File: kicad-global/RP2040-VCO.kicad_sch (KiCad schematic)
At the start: 57 parts, among them J1 Out, J2 Conn_01x06_Female, J3 Conn_01x06_Male, J4 Conn_01x08_Female, J5 Conn_01x08_Male, J6 V/oct, J7 Inv CV, J8 Power Input, SW1 SW_MEC_LOW_PROF_LED, SW2 SW_SPDT, U1 TL074, U2 Seed_XIAO_RP2040, U3 AP2210K-5.0TRG1

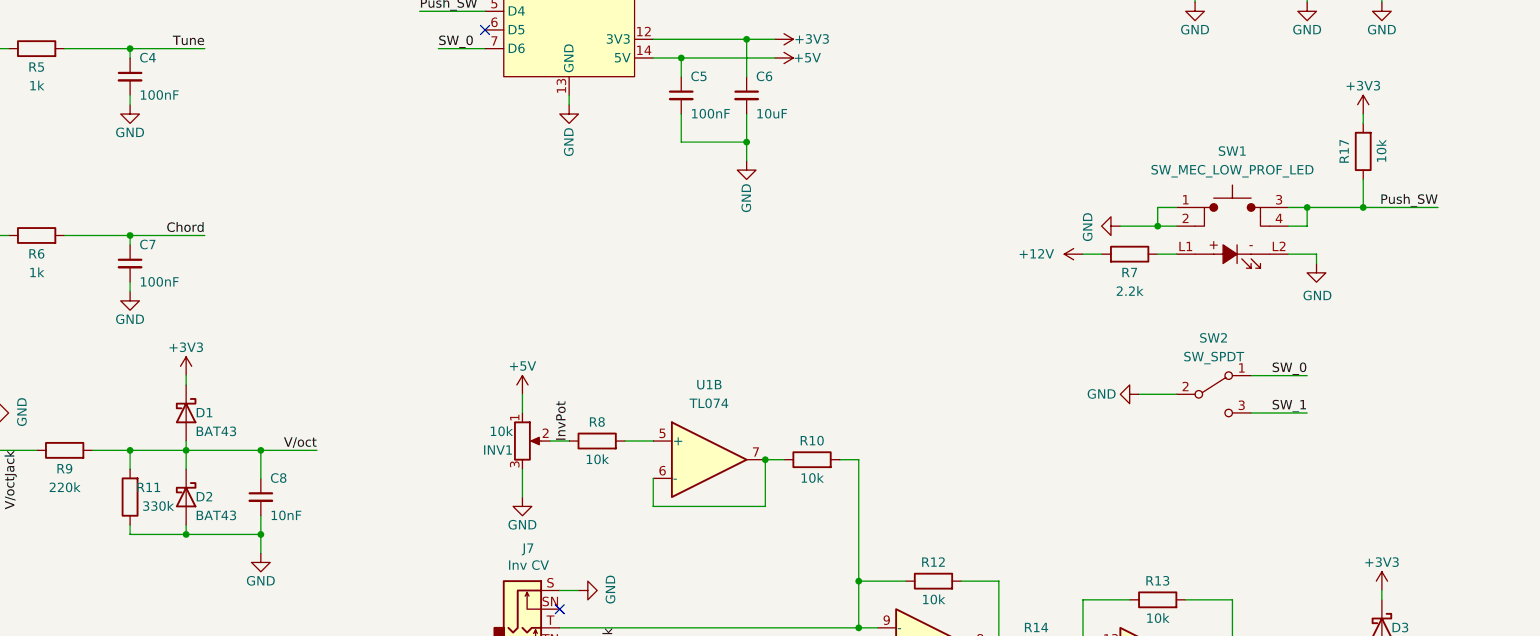
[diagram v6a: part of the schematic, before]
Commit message: update pcb to v1.2 to fix switch issue with switch LED
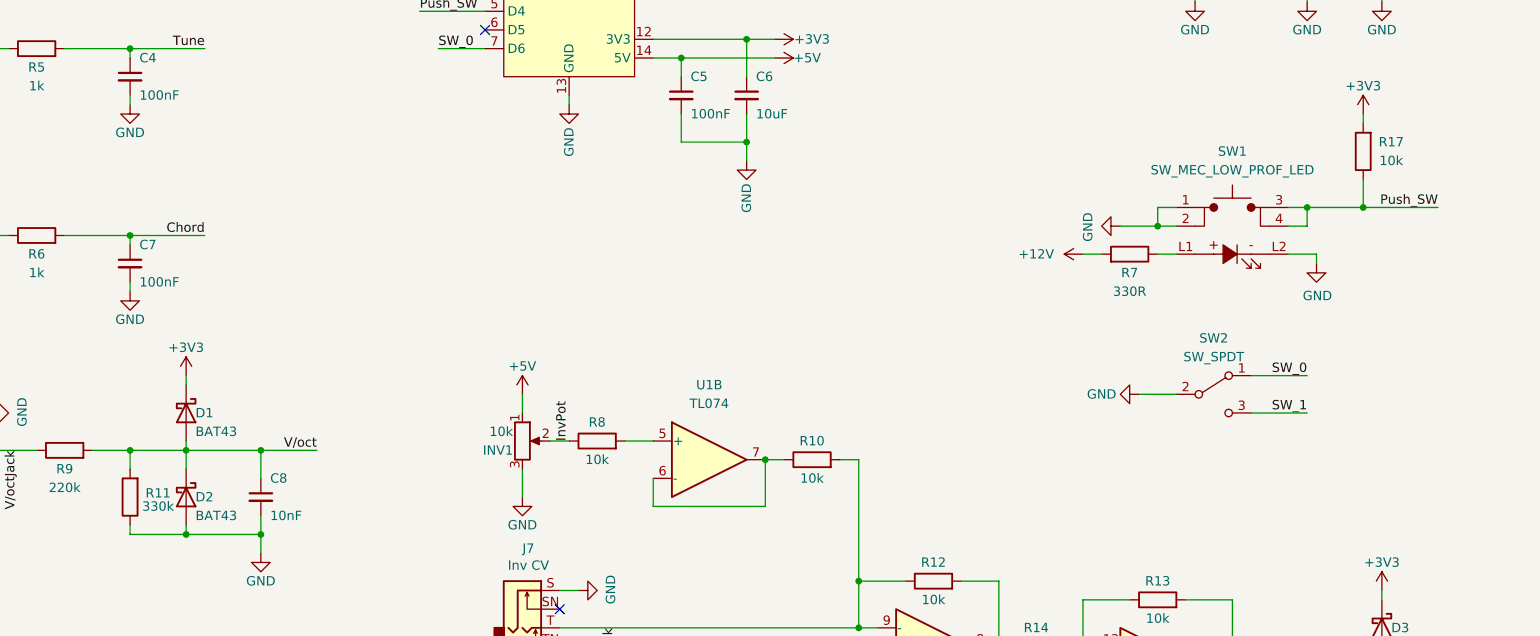
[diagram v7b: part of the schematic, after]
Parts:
- R7: value 2.2k -> 330R; MFP RC0805FR-132K2L -> RC0805FR-10330RL
- U3: MFP (none) -> AP2210K-5.0TRG1; MPN AP2210K-5.0TRG1 -> (none)
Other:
- company: (none) -> Bleep Sound
- title: (none) -> RP2040 VCO
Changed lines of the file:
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@@
 (kicad_sch (version 20230121) (generator eeschema)
   (paper "A4")
+  (title_block
+    (title "RP2040 VCO")
+    (date "2023-10-11")
+    (rev "1.2")
+    (company "Bleep Sound")
+  )
   (junction (at 123.19 175.26) (diameter 0) (color 0 0 0 0)
   )
@@
   (junction (at 143.51 187.96) (diameter 0) (color 0 0 0 0)
   )
-  (junction (at 214.63 81.28) (diameter 0) (color 0 0 0 0)
-  )
   (junction (at 130.81 58.42) (diameter 0) (color 0 0 0 0)
   )
@@
   (junction (at 236.22 46.99) (diameter 0) (color 0 0 0 0)
   )
+  (junction (at 214.63 81.28) (diameter 0) (color 0 0 0 0)
+  )
   (junction (at 26.67 33.02) (diameter 0) (color 0 0 0 0)
   )
@@
     (stroke (width 0) (type default))
   )
+  (wire (pts (xy 214.63 81.28) (xy 224.79 81.28))
+    (stroke (width 0) (type default))
+  )
   (wire (pts (xy 207.01 104.14) (xy 199.39 104.14))
     (stroke (width 0) (type default))
@@
     (stroke (width 0) (type default))
   )
-  (wire (pts (xy 214.63 68.58) (xy 214.63 69.85))
-    (stroke (width 0) (type default))
-  )
   (wire (pts (xy 143.51 115.57) (xy 146.05 115.57))
     (stroke (width 0) (type default))
@@
     (stroke (width 0) (type default))
   )
+  (wire (pts (xy 214.63 68.58) (xy 214.63 69.85))
+    (stroke (width 0) (type default))
+  )
   (wire (pts (xy 166.37 175.26) (xy 168.91 175.26))
     (stroke (width 0) (type default))
@@
     (stroke (width 0) (type default))
   )
+  (wire (pts (xy 214.63 77.47) (xy 214.63 81.28))
+    (stroke (width 0) (type default))
+  )
   (wire (pts (xy 148.59 143.51) (xy 146.05 143.51))
     (stroke (width 0) (type default))
@@
     (stroke (width 0) (type default))
   )
-  (wire (pts (xy 214.63 81.28) (xy 224.79 81.28))
-    (stroke (width 0) (type default))
-  )
   (wire (pts (xy 39.37 182.88) (xy 45.72 182.88))
     (stroke (width 0) (type default))
@@
     (stroke (width 0) (type default))
   )
-  (wire (pts (xy 214.63 77.47) (xy 214.63 81.28))
-    (stroke (width 0) (type default))
-  )
   (wire (pts (xy 236.22 46.99) (xy 236.22 36.83))
     (stroke (width 0) (type default))
@@
       (effects (font (size 1.27 1.27)))
     )
-    (property "Value" "2.2k" (at 182.88 92.71 90)
+    (property "Value" "330R" (at 182.88 92.71 90)
       (effects (font (size 1.27 1.27)))
     )
@@
       (effects (font (size 1.27 1.27)) hide)
     )
-    (property "MFP" "RC0805FR-132K2L" (at 182.88 87.63 0)
+    (property "MFP" "RC0805FR-10330RL" (at 182.88 87.63 0)
       (effects (font (size 1.27 1.27)) hide)
     )
@@
     )
   )
+  (symbol (lib_id "Device:R") (at 214.63 73.66 180) (unit 1)
+    (in_bom yes) (on_board yes) (dnp no)
+    (property "Reference" "R17" (at 218.44 72.39 0)
+      (effects (font (size 1.27 1.27)))
+    )
+    (property "Value" "10k" (at 218.44 74.93 0)
+      (effects (font (size 1.27 1.27)))
+    )
+    (property "Footprint" "Resistor_SMD:R_0805_2012Metric_Pad1.20x1.40mm_HandSolder" (at 216.408 73.66 90)
+      (effects (font (size 1.27 1.27)) hide)
+    )
+    (property "Datasheet" "~" (at 214.63 73.66 0)
+      (effects (font (size 1.27 1.27)) hide)
+    )
+    (property "Comment " "1/4W, 1%" (at 214.63 73.66 0)
+      (effects (font (size 1.27 1.27)) hide)
+    )
+    (property "MFN" "YAGEO" (at 214.63 73.66 0)
+      (effects (font (size 1.27 1.27)) hide)
+    )
+    (property "MFP" "RC0805FR-1010KL" (at 214.63 73.66 0)
+      (effects (font (size 1.27 1.27)) hide)
+    )
+    (pin "1")
+    (pin "2")
+    (instances
+      (project "RP2040-VCO"
+        (path "/fea7c5d1-76d6-41a0-b5e3-29889dbb8ce0"
+          (reference "R17") (unit 1)
+        )
+      )
+    )
+  )
   (symbol (lib_id "Amplifier_Operational:TL074") (at 125.73 115.57 0) (unit 2)
     (in_bom yes) (on_board yes) (dnp no) (fields_autoplaced)
@@
     )
   )
+  (symbol (lib_id "power:+3V3") (at 214.63 68.58 0) (unit 1)
+    (in_bom yes) (on_board yes) (dnp no)
+    (property "Reference" "#PWR048" (at 214.63 72.39 0)
+      (effects (font (size 1.27 1.27)) hide)
+    )
+    (property "Value" "+3V3" (at 214.63 64.77 0)
+      (effects (font (size 1.27 1.27)))
+    )
+    (property "Footprint" "" (at 214.63 68.58 0)
+      (effects (font (size 1.27 1.27)) hide)
+    )
+    (property "Datasheet" "" (at 214.63 68.58 0)
+      (effects (font (size 1.27 1.27)) hide)
+    )
+    (pin "1")
+    (instances
+      (project "RP2040-VCO"
+        (path "/fea7c5d1-76d6-41a0-b5e3-29889dbb8ce0"
+          (reference "#PWR048") (unit 1)
+        )
+      )
+    )
+  )
   (symbol (lib_id "power:+5V") (at 266.7 87.63 270) (mirror x) (unit 1)
     (in_bom yes) (on_board yes) (dnp no)
@@
   (symbol (lib_id "Device:R") (at 46.99 120.65 180) (unit 1)
     (in_bom yes) (on_board yes) (dnp no)
-    (property "Reference" "R11" (at 49.53 119.38 0)
-      (effects (font (size 1.27 1.27)))
+    (property "Reference" "R11" (at 50.8 119.38 0)
+      (effects (font (size 1.27 1.27)) (justify bottom))
     )
     (property "Value" "330k" (at 50.8 121.92 0)
@@
     )
   )
-  (symbol (lib_id "Device:R") (at 214.63 73.66 180) (unit 1)
-    (in_bom yes) (on_board yes) (dnp no)
-    (property "Reference" "R17" (at 212.09 73.66 90)
-      (effects (font (size 1.27 1.27)))
-    )
-    (property "Value" "10k" (at 217.17 73.66 90)
-      (effects (font (size 1.27 1.27)))
-    )
-    (property "Footprint" "Resistor_SMD:R_0805_2012Metric_Pad1.20x1.40mm_HandSolder" (at 216.408 73.66 90)
-      (effects (font (size 1.27 1.27)) hide)
-    )
-    (property "Datasheet" "~" (at 214.63 73.66 0)
-      (effects (font (size 1.27 1.27)) hide)
-    )
-    (property "Comment " "1/4W, 1%" (at 214.63 73.66 0)
-      (effects (font (size 1.27 1.27)) hide)
-    )
-    (property "MFN" "YAGEO" (at 214.63 73.66 0)
-      (effects (font (size 1.27 1.27)) hide)
-    )
-    (property "MFP" "RC0805FR-1010KL" (at 214.63 73.66 0)
-      (effects (font (size 1.27 1.27)) hide)
-    )
-    (pin "1")
-    (pin "2")
-    (instances
-      (project "RP2040-VCO"
-        (path "/fea7c5d1-76d6-41a0-b5e3-29889dbb8ce0"
-          (reference "R17") (unit 1)
-        )
-      )
-    )
-  )
   (symbol (lib_id "power:+12V") (at 100.33 168.91 0) (unit 1)
     (in_bom yes) (on_board yes) (dnp no)
@@
       (effects (font (size 1.27 1.27)) (justify left) hide)
     )
-    (property "MPN" "AP2210K-5.0TRG1" (at 167.64 182.88 0)
-      (effects (font (size 1.27 1.27)) (justify left) hide)
+    (property "MFP" "AP2210K-5.0TRG1" (at 143.51 177.8 0)
+      (effects (font (size 1.27 1.27)) hide)
     )
     (pin "1")
@@
     )
   )
-  (symbol (lib_id "power:+3V3") (at 214.63 68.58 0) (unit 1)
-    (in_bom yes) (on_board yes) (dnp no)
-    (property "Reference" "#PWR048" (at 214.63 72.39 0)
-      (effects (font (size 1.27 1.27)) hide)
-    )
-    (property "Value" "+3V3" (at 214.63 64.77 0)
-      (effects (font (size 1.27 1.27)))
-    )
-    (property "Footprint" "" (at 214.63 68.58 0)
-      (effects (font (size 1.27 1.27)) hide)
-    )
-    (property "Datasheet" "" (at 214.63 68.58 0)
-      (effects (font (size 1.27 1.27)) hide)
-    )
-    (pin "1")
-    (instances
-      (project "RP2040-VCO"
-        (path "/fea7c5d1-76d6-41a0-b5e3-29889dbb8ce0"
-          (reference "#PWR048") (unit 1)
-        )
-      )
-    )
-  )
   (symbol (lib_id "Device:C_Small") (at 166.37 180.34 0) (mirror y) (unit 1)
     (in_bom yes) (on_board yes) (dnp no)
@@
       (effects (font (size 1.27 1.27)) hide)
     )
-    (property "Datasheet" "~" (at 194.31 106.68 0)
+    (property "Datasheet" "https://www.taydaelectronics.com/mini-toggle-switch-1m-series-spdt-on-off-on.html" (at 194.31 106.68 0)
       (effects (font (size 1.27 1.27)) hide)
     )

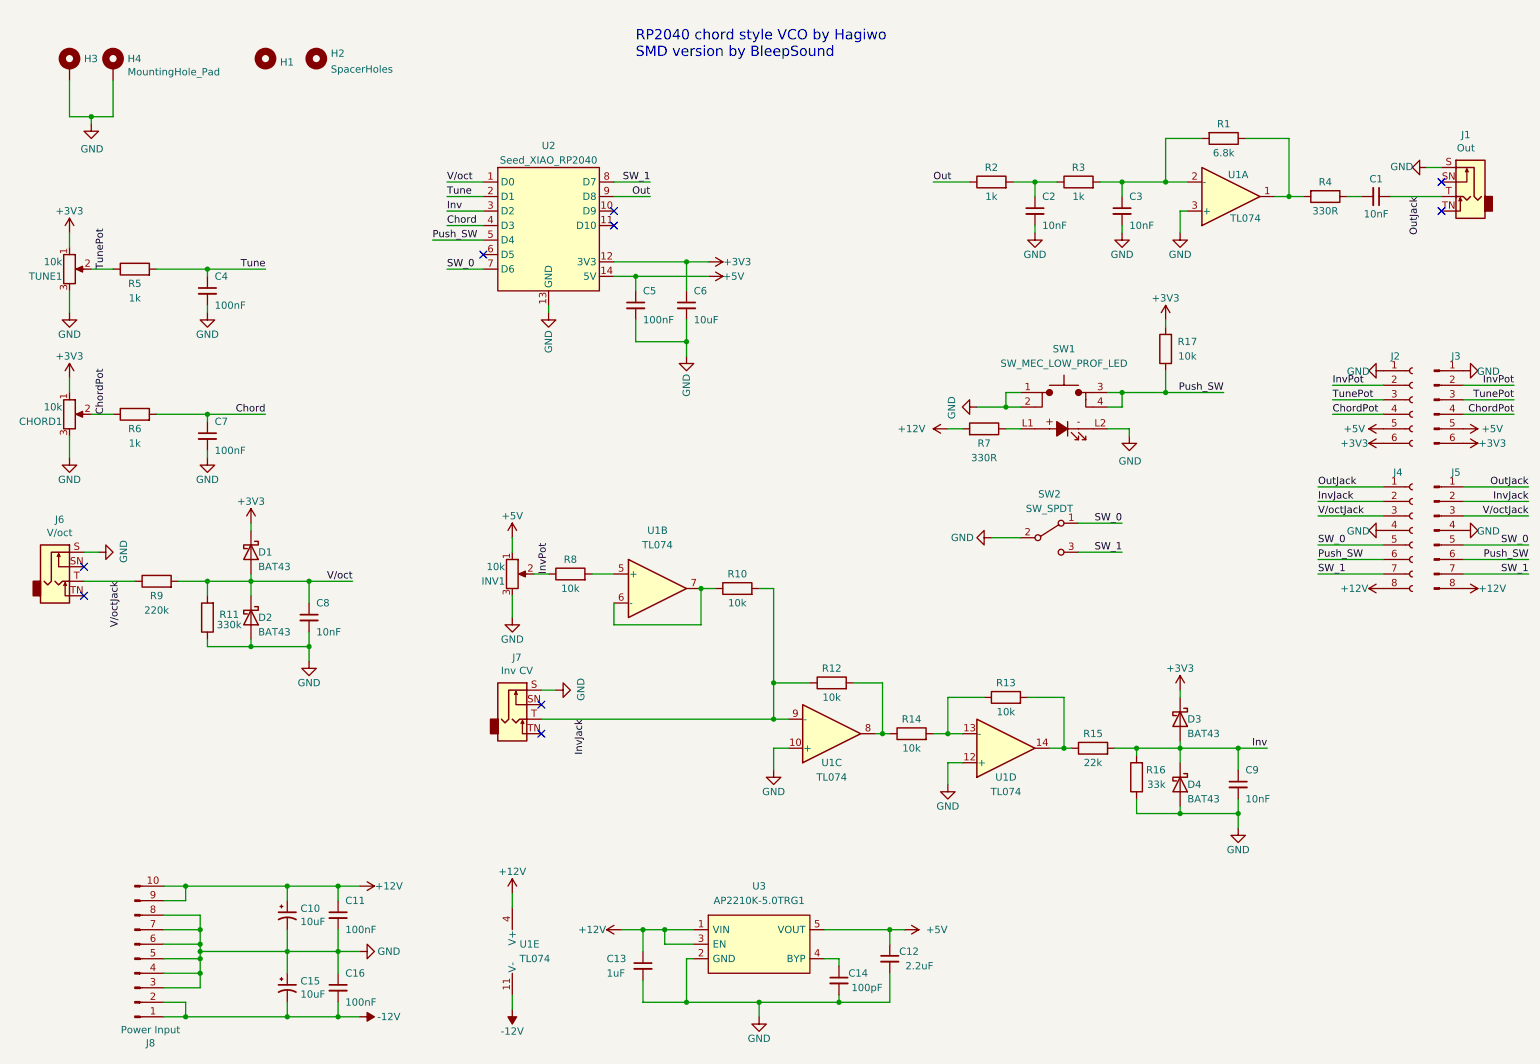
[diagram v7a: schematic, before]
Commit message: V1.4 update
add extra 10k resistor on inv CV input (missing)
Update BoM for clarity
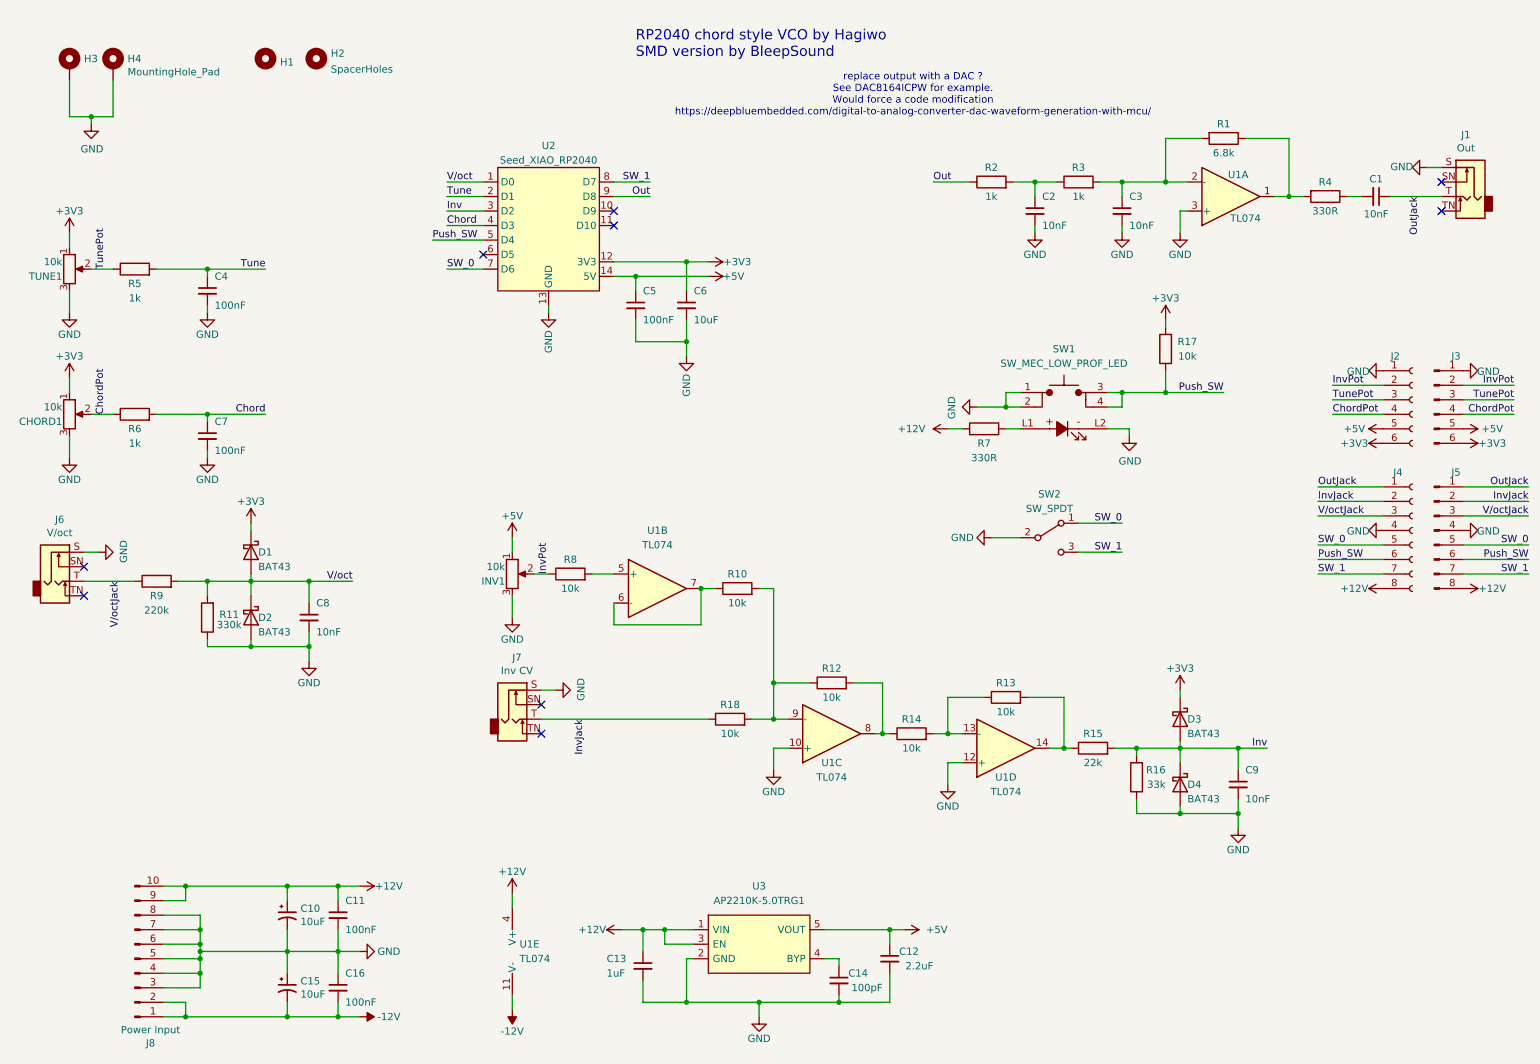
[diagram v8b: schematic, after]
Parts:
- added R18: 10k, Resistor_SMD:R_0805_2012Metric_Pad1.20x1.40mm_HandSolder, symbol Device:R
- C1, C2, C3, C8, C9: MFN Samsung Electro-Mechanics -> (none); MFP CL21B103KAANNNC -> (none); manf (none) -> Samsung Electro-Mechanics; manf# (none) -> CL21B103KAANNNC
- C10, C15: Links (none) -> Mouser/RS/Digikey; MFN Kemet -> (none); MFP EXV106M025S9BAA -> (none); manf (none) -> Kemet; manf# (none) -> EXV106M025S9BAA
- C11, C16, C4, C5, C7: Links (none) -> Mouser/RS/Digikey; MFN Kemet -> (none); MFP C0805C104M3RAC7210 -> (none); manf (none) -> Kemet; manf# (none) -> C0805C104M3RAC7210
- C12: Links (none) -> Mouser/RS/Digikey; MFN Samsung Electro-Mechanics -> (none); MFP CL21A225KAFNNNE -> (none); manf (none) -> Samsung Electro-Mechanics; manf# (none) -> CL21A225KAFNNNE
- C13: Links (none) -> Mouser/RS/Digikey; MFN Samsung Electro-Mechanics -> (none); MFP CL21B105KAFNFNE -> (none); manf (none) -> Samsung Electro-Mechanics; manf# (none) -> CL21B105KAFNFNE
- C14: Links (none) -> Mouser/RS/Digikey; MFN Wurth Elektronik -> (none); MFP 885012207054 -> (none); manf (none) -> Wurth Elektronik; manf# (none) -> 885012207054
- C6: Links (none) -> Mouser/RS/Digikey; MFN Samsung Electro-Mechanics -> (none); MFP CL21A106KAYNNNE -> (none); manf (none) -> Samsung Electro-Mechanics; manf# (none) -> CL21A106KAYNNNE
- CHORD1, INV1, TUNE1: Links (none) -> https://www.thonk.co.uk/shop/alpha-9mm-pots/
- D1, D2, D3, D4: Links (none) -> Mouser/RS/Digikey; MFN Panjit -> (none); MFP BAT43W_R1_00001 -> (none); manf (none) -> Panjit; manf# (none) -> BAT43W_R1_00001
- J1, J6, J7: Links (none) -> https://www.thonk.co.uk/shop/thonkiconn/
- J8: Links (none) -> https://www.thonk.co.uk/shop/eurorack-diy-essentials/
- R1: Links (none) -> Mouser/RS/Digikey; MFN KOA Speer -> (none); MFP RK73B2ATTDD682J -> (none); manf (none) -> KOA Speer; manf# (none) -> RK73B2ATTDD682J
- R10, R12, R13, R14, R17, R8: Links (none) -> Mouser/RS/Digikey; MFN YAGEO -> (none); MFP RC0805FR-1010KL -> (none); manf (none) -> YAGEO; manf# (none) -> RC0805FR-1010KL
- R11: Links (none) -> Mouser/RS/Digikey; MFN KOA Speer -> (none); MFP RK73H2ATTD3303F -> (none); manf (none) -> KOA Speer; manf# (none) -> RK73H2ATTD3303F
- R15: Links (none) -> Mouser/RS/Digikey; MFN YAGEO -> (none); MFP RC0805FR-1322KL -> (none); manf (none) -> YAGEO; manf# (none) -> RC0805FR-1322KL
- R16: Links (none) -> Mouser/RS/Digikey; MFN KOA Speer -> (none); MFP RK73H2ATTD3302F -> (none); manf (none) -> KOA Speer; manf# (none) -> RK73H2ATTD3302F
- R2, R3, R5, R6: Links (none) -> Mouser/RS/Digikey; MFN KOA Speer -> (none); MFP RK73H2ATTE1001F -> (none); manf (none) -> KOA Speer; manf# (none) -> RK73H2ATTE1001F
- R4, R7: Links (none) -> Mouser/RS/Digikey; MFN YAGEO -> (none); MFP RC0805FR-10330RL -> (none); manf (none) -> YAGEO; manf# (none) -> RC0805FR-10330RL
- R9: Links (none) -> Mouser/RS/Digikey; MFN YAGEO -> (none); MFP RC0805FR-13220KL -> (none); manf (none) -> YAGEO; manf# (none) -> RC0805FR-13220KL
- SW1: Links (none) -> https://www.thonk.co.uk/shop/low-profile-led-buttons/; MFN THONK -> (none); MFP Low-Profile LED Buttons -> (none); manf (none) -> THONK; manf# (none) -> Low-Profile LED Buttons
- SW2: Links (none) -> https://www.taydaelectronics.com/mini-toggle-switch-1m-seri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; manf# (none) -> SPDT On-Off-On switch
- U1: Links (none) -> Mouser/RS/Digikey; MFN Texas Instrument -> (none); MFP TL074CDR -> (none); manf (none) -> Texas Instrument; manf# (none) -> TL074CDR
- U2: Links (none) -> https://www.amazon.co.uk/Microcontroller-Dual-Core-MicroPyt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; MFN Seeed Studio -> (none); MFP Seeed Studio XIAO RP2040 -> (none); manf (none) -> Seeed Studio; manf# (none) -> Seeed Studio XIAO RP2040
- U3: Links (none) -> Mouser/RS/Digikey; MFN Diodes Inc. -> (none); MFP AP2210K-5.0TRG1 -> (none); manf (none) -> Diodes Inc.; manf# (none) -> AP2210K-5.0TRG1
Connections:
- net InvJack: now also R18.1; no longer R10.2, R12.1, U1.9 (-)
- new net: R10.2, R12.1, R18.2, U1.9 (-)
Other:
- note added: "replace output with a DAC ? See DAC8164ICPW for example. Would force a code modification https://deepbluembedded.com/digital-to-analog-converter-dac-waveform-generation-with-mcu/"
